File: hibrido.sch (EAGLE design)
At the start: 14 parts

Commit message: Hibrido casi terminado, sin considerar comunicación entre ESPs
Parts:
- removed D1: M2, SamacSys_Parts:M2
- removed IMU: (no value), MPU6050:MPU6050
- removed MOTOR2: MOTOR_JGB370, MOTOR_JGB370:MOTOR_JGB370
- removed MOTOR_1, MOTOR_2: (no value), jst-ph:JST-PH6
- added A1: TEENSY_4.1, TEENSY_4.1:TEENSY_4.1
- added ABAJO, ARRIBA: (no value), pinhead:PINHD-1X4
- added ALIMENTACION_DRIVER, DRIVER_HIBRIDACION: (no value), con-ptr500:AK500/2-H
- added BNO055: BNO055, BNO055:BNO055
- added D2: 1N4004, diode:1N4004
- added JP1, JP5, JP6: (no value), pinhead:PINHD-1X2
- added JP2, JP3, JP4: (no value), pinhead:PINHD-1X3
- added MOTOR3, MOTOR5: MOTOR_JGB370, MOTOR_JGB370:MOTOR_JGB370
- added U$3: TB6612FNG, TB6612FNG:TB6612FNG
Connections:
- net ENAM1 renamed C1_H
- net ENBM1 renamed C2_H
- removed net +3V3: IMU.VCC, MOTOR1.+5V, MOTOR2.+5V, MOTOR_1.5, MOTOR_2.5
- removed net 16.8V: LED_GREEN.A, RELAYG$2.NO, U$2.IN+
- removed net ENAM2: MOTOR2.ENCB
- removed net ENBM2: MOTOR2.ENCA
- removed net INT_MPU: IMU.INT
- removed net MA_1: MOTOR1.MOTOR-
- removed net MA_2: MOTOR2.MOTOR-
- removed net MB_1: MOTOR1.MOTOR+
- removed net MB_2: MOTOR2.MOTOR+
- new net 12V: ALIMENTACION_DRIVER-1.KL, LED_GREEN.A, RELAYG$2.NO, U$2.IN+, U$3.VM
- new net 14: A1.A0, JP4.1
- new net 16: A1.A2, JP6.1
- new net 17: A1.A3, JP6.2
- new net 24: A1.A10, JP5.1
- new net 25: A1.A11, JP5.2
- new net 3V3: A1.3.3V, BNO055.3V3, JP2.2, JP3.2, JP4.2, MOTOR1.+5V, MOTOR3.ENCA, MOTOR5.ENCA
- new net 5V: ABAJO.3, ARRIBA.1, ARRIBA.3, JP1.2, U$2.OUT+, U$3.ST/BY, U$3.VCC
- new net 7: A1.D7, JP2.1
- new net 8: A1.D8, JP3.1
- new net AI1: A1.A9, U$3.AI1
- new net AI2: A1.A8, U$3.AI2
- new net BI1: A1.D9, U$3.BI1
- new net BI2: A1.(CS)D10, U$3.BI2
- new net LPWM: A1.(SDO)D11, ABAJO.4
- new net L_IS: A1.A17, ABAJO.2
- new net N$1: LED_RED.C, R1.2
- new net N$10: A1.D28
- new net N$11: A1.(CLK)D13
- new net N$19: A1.D5
- new net N$2: A1.D34
- new net N$24: A1.A7
- new net N$25: A1.A6
- new net N$3: A1.D35
- new net N$30: A1.A1
- new net N$33: A1.A16
- new net N$34: A1.A15
- new net N$35: A1.A14
- new net N$38: A1.A12
- new net N$39: A1.A13
- new net N$4: LED_GREEN.C, R2.2
- new net N$6: A1.D32
- new net N$7: A1.D31
- new net N$8: A1.D30
- new net N$9: A1.D29
- new net OUTA: DRIVER_HIBRIDACION-2.KL, MOTOR1.MOTOR+
- new net OUTB: DRIVER_HIBRIDACION-1.KL, MOTOR1.MOTOR-
- new net PWMA: A1.D37, U$3.PWMA
- new net PWMB: A1.D36, U$3.PWMB
- new net RPWM: A1.D33, ARRIBA.4
- new net R_IS: A1.(SDI)D12, ARRIBA.2
- new net VIN_TEENSY: A1.VIN, JP1.1
- net A01: now also MOTOR3.MOTOR+, U$3.A01; no longer MOTOR_1.1
- net A02: now also MOTOR3.ENCB, U$3.A02; no longer MOTOR_1.6
- net B01: now also MOTOR5.ENCB, U$3.B01; no longer MOTOR_2.6
- net B02: now also MOTOR5.MOTOR+, U$3.B02; no longer MOTOR_2.1
- net C1_L: now also A1.D6, MOTOR5.GND; no longer MOTOR_2.3
- net C1_R: now also A1.D3, MOTOR3.GND; no longer MOTOR_1.3
- net C2_L: now also A1.D4, MOTOR5.+5V; no longer MOTOR_2.4
- net C2_R: now also A1.D2, MOTOR3.+5V; no longer MOTOR_1.4
- net GND: now also A1.GND, ABAJO.1, ALIMENTACION_DRIVER-2.KL, BNO055.GND, D2.A, JP2.3, JP3.3, JP4.3, MOTOR3.MOTOR-, MOTOR5.MOTOR-, U$2.OUT-, U$3.GND@16, U$3.GND@3, U$3.GND@8; no longer D1.A, IMU.GND, MOTOR2.GND, MOTOR_1.2, MOTOR_2.2
- net SCL: now also A1.A5, BNO055.SCL; no longer IMU.SCL
- net SDA: now also A1.A4, BNO055.SDA; no longer IMU.SDA
- net VSWITCH: now also D2.C; no longer D1.K
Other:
- note added: "MOTOR HIBRIDACIÓN"
- note added: "PINES EXTRAS"
- note added: "SEÑALES MANDO"
- note removed: "11/02/25"
- note removed: "20203884"
- note removed: "MOTORES 2 (ESPADINES 2.54MM)"

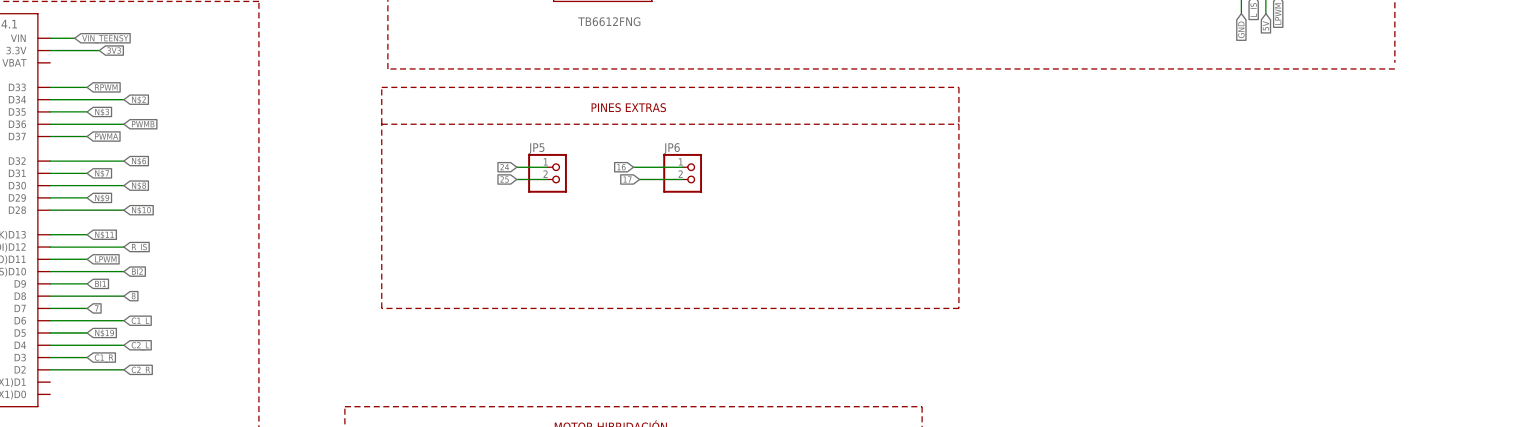
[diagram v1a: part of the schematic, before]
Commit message: PCB antes del cambio del drill vias
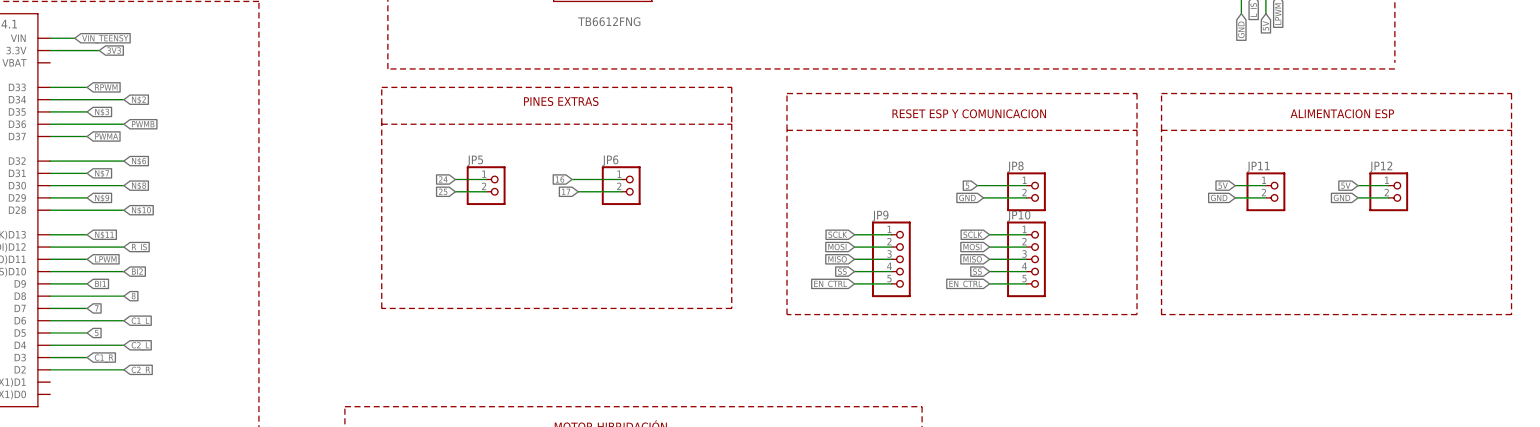
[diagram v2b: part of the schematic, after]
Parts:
- added JP10, JP9: (no value), pinhead:PINHD-1X5
- added JP11, JP12, JP8: (no value), pinhead:PINHD-1X2
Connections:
- removed net N$19: A1.D5
- new net 5: A1.D5, JP8.1
- new net EN_CTRL: JP10.5, JP9.5
- new net MISO: JP10.3, JP9.3
- new net MOSI: JP10.2, JP9.2
- new net SCLK: JP10.1, JP9.1
- new net SS: JP10.4, JP9.4
- net 5V: now also JP11.1, JP12.1
- net GND: now also JP11.2, JP12.2, JP8.2
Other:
- note added: "ALIMENTACION ESP"
- note added: "RESET ESP Y COMUNICACION"
- moved on the sheet: JP5, JP6

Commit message: Version final de la PCB, falta revisar por los demás
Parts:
- REG: SPICEPREFIX (none) -> E
- renumbered U$2 to REG
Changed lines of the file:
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@@
 <setting verticaltext="up"/>
 </settings>
-<grid distance="0.05" unitdist="inch" unit="inch" style="lines" multiple="1" display="no" altdistance="0.01" altunitdist="inch" altunit="inch"/>
+<grid distance="0.1" unitdist="inch" unit="inch" style="lines" multiple="1" display="no" altdistance="0.01" altunitdist="inch" altunit="inch"/>
 <layers>
 <layer number="1" name="Top" color="4" fill="1" visible="no" active="no"/>
@@
 <part name="BAT" library="con-ptr500" library_urn="urn:adsk.eagle:library:181" deviceset="AK500/2-H" device="" package3d_urn="urn:adsk.eagle:package:9901/1"/>
 <part name="GND10" library="supply1" library_urn="urn:adsk.eagle:library:371" deviceset="GND" device=""/>
-<part name="U$2" library="userlib" deviceset="CP8-ADJ" device=""/>
+<part name="REG" library="userlib" deviceset="CP8-ADJ" device="">
+<attribute name="SPICEPREFIX" value="E"/>
+</part>
 <part name="LED_RED" library="led" library_urn="urn:adsk.eagle:library:259" deviceset="LED" device="5MM" package3d_urn="urn:adsk.eagle:package:15799/2"/>
 <part name="LED_GREEN" library="led" library_urn="urn:adsk.eagle:library:259" deviceset="LED" device="5MM" package3d_urn="urn:adsk.eagle:package:15799/2"/>
@@
 <attribute name="VALUE" x="-486.41" y="92.71" size="1.778" layer="96"/>
 </instance>
-<instance part="U$2" gate="G$1" x="-337.82" y="114.3" smashed="yes"/>
+<instance part="REG" gate="G$1" x="-337.82" y="114.3" smashed="yes"/>
 <instance part="LED_RED" gate="G$1" x="-261.62" y="127" smashed="yes">
 <attribute name="NAME" x="-258.064" y="122.428" size="1.778" layer="95" rot="R90"/>
@@
 </segment>
 <segment>
-<pinref part="U$2" gate="G$1" pin="IN-"/>
+<pinref part="REG" gate="G$1" pin="IN-"/>
 <wire x1="-352.806" y1="111.76" x2="-355.6" y2="111.76" width="0.1524" layer="91"/>
 <pinref part="GND4" gate="1" pin="GND"/>
@@
 </segment>
 <segment>
-<pinref part="U$2" gate="G$1" pin="OUT-"/>
+<pinref part="REG" gate="G$1" pin="OUT-"/>
 <pinref part="GND1" gate="1" pin="GND"/>
 <wire x1="-322.326" y1="111.76" x2="-322.326" y2="100.33" width="0.1524" layer="91"/>
@@
 </segment>
 <segment>
-<pinref part="U$2" gate="G$1" pin="IN+"/>
+<pinref part="REG" gate="G$1" pin="IN+"/>
 <wire x1="-352.806" y1="116.84" x2="-355.6" y2="116.84" width="0.1524" layer="91"/>
 <wire x1="-355.6" y1="116.84" x2="-355.6" y2="121.92" width="0.1524" layer="91"/>
@@
 <net name="5V" class="0">
 <segment>
-<pinref part="U$2" gate="G$1" pin="OUT+"/>
+<pinref part="REG" gate="G$1" pin="OUT+"/>
 <wire x1="-322.326" y1="116.84" x2="-312.42" y2="116.84" width="0.1524" layer="91"/>
 <label x="-312.42" y="116.84" size="1.27" layer="95" xref="yes"/>
